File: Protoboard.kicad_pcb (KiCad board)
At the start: 2 copper layers, 99 x 138 mm, 76 parts, among them P1 CONN_01X08, P2 CONN_01X04, P3 CONN_01X05, P5 CONN_02X05, U1 LoLin_V3

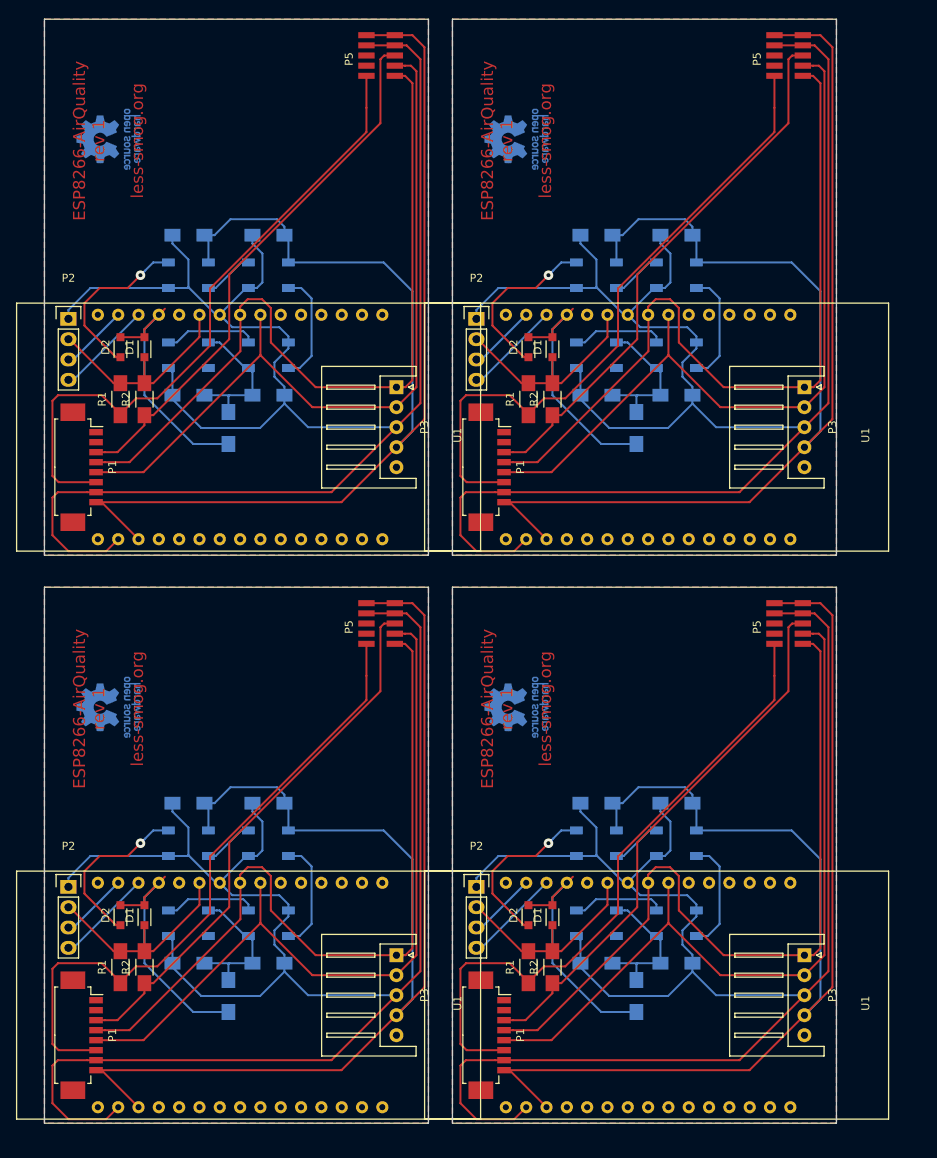
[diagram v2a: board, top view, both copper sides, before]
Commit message: Removed gerber files.
This is rev 2
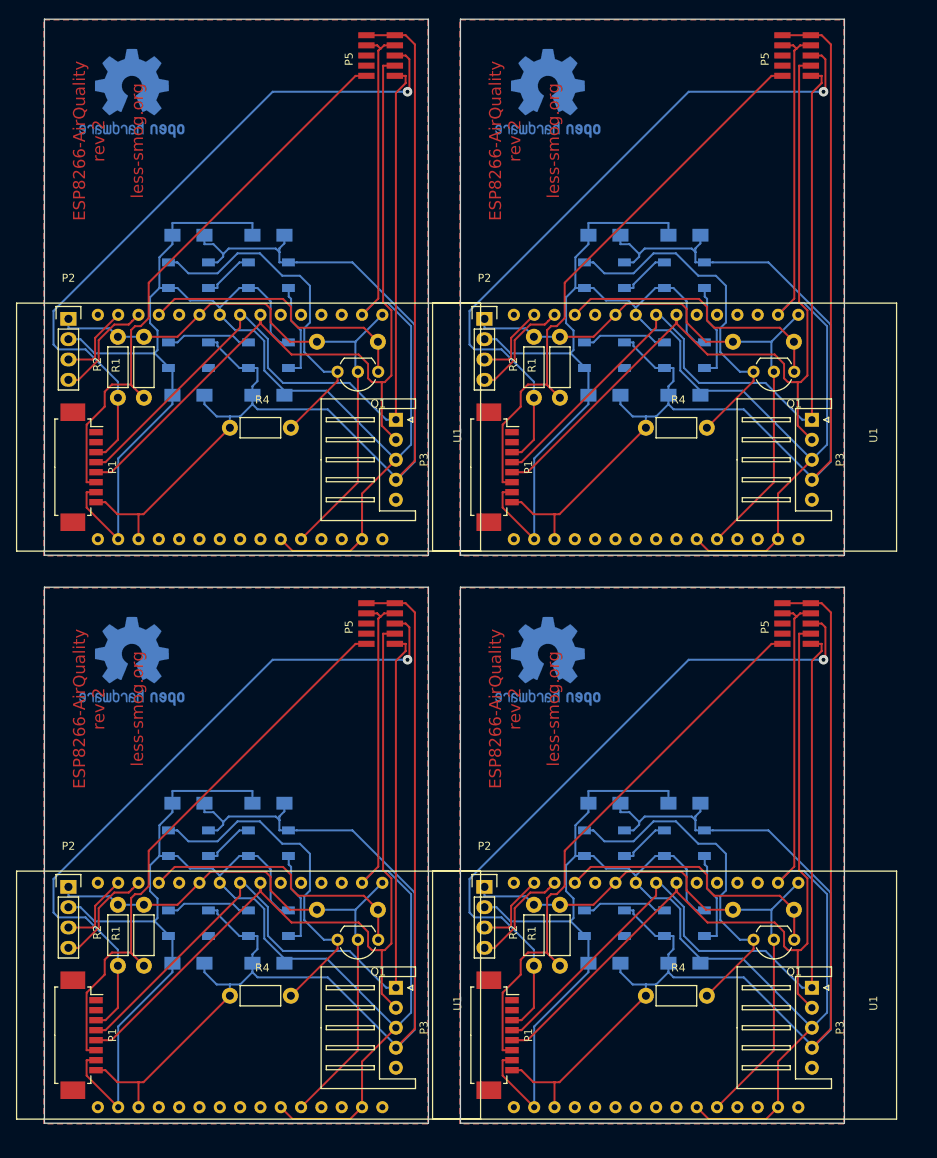
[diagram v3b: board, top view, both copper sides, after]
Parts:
- removed the C1 at (88.1, 117.9)
- removed the C1 at (88.1, 46.9)
- removed the C2 at (98.1, 117.9)
- removed the C2 at (98.1, 46.9)
- removed the C3 at (98.1, 137.9)
- removed the C3 at (98.1, 66.9)
- removed the C4 at (88.1, 137.9)
- removed the C4 at (88.1, 66.9)
- removed D1 (x4), D2 (x4): D, Diodes_SMD:SOD-323_HandSoldering
- removed the LED1 at (88.1, 122.9)
- removed the LED1 at (88.1, 51.9)
- removed the LED2 at (98.1, 122.9)
- removed the LED2 at (98.1, 51.9)
- removed the LED3 at (98.1, 132.9)
- removed the LED3 at (98.1, 61.9)
- removed the LED4 at (88.1, 132.9)
- removed the LED4 at (88.1, 61.9)
- removed the P1 at (75.1, 146.9)
- removed the P1 at (75.1, 75.9)
- removed the P2 at (73.1, 128.4)
- removed the P2 at (73.1, 57.4)
- removed the P3 at (114.1, 136.9)
- removed the P3 at (63.1, 136.9)
- removed the P3 at (114.1, 65.9)
- removed the P5 at (110.3, 92.9)
- removed the P5 at (110.3, 21.9)
- removed the R1 at (79.6, 138.4)
- removed the R1 at (28.6, 138.4)
- removed the R1 at (79.6, 67.4)
- removed the R1 at (28.6, 67.4)
- removed the R2 at (82.6, 138.4)
- removed the R2 at (31.6, 138.4)
- removed the R2 at (82.6, 67.4)
- removed the R2 at (31.6, 67.4)
- removed the R3 at (93.1, 142.0)
- removed the R3 at (42.1, 142.0)
- removed the R3 at (93.1, 71.0)
- removed the R3 at (42.1, 71.0)
- removed the REF*** at (78.1, 105.9)
- removed the REF*** at (27.1, 105.9)
- removed the REF*** at (78.1, 34.9)
- removed the REF*** at (27.1, 34.9)
- removed the U1 at (66.6, 157.7)
- removed the U1 at (66.6, 86.7)
- added C1: 100nF, Capacitors_SMD:C_1206_HandSoldering, B.Cu at (89.1, 117.9)
- added C1: 100nF, Capacitors_SMD:C_1206_HandSoldering, B.Cu at (89.1, 46.9)
- added C2: 100nF, Capacitors_SMD:C_1206_HandSoldering, B.Cu at (99.1, 117.9)
- added C2: 100nF, Capacitors_SMD:C_1206_HandSoldering, B.Cu at (99.1, 46.9)
- added C3: 100nF, Capacitors_SMD:C_1206_HandSoldering, B.Cu at (99.1, 137.9)
- added C3: 100nF, Capacitors_SMD:C_1206_HandSoldering, B.Cu at (99.1, 66.9)
- added C4: 100nF, Capacitors_SMD:C_1206_HandSoldering, B.Cu at (89.1, 137.9)
- added C4: 100nF, Capacitors_SMD:C_1206_HandSoldering, B.Cu at (89.1, 66.9)
- added LED1: WS2812B, LEDs:LED_WS2812B-PLCC4, B.Cu at (89.1, 122.9)
- added LED1: WS2812B, LEDs:LED_WS2812B-PLCC4, B.Cu at (89.1, 51.9)
- added LED2: WS2812B, LEDs:LED_WS2812B-PLCC4, B.Cu at (99.1, 122.9)
- added LED2: WS2812B, LEDs:LED_WS2812B-PLCC4, B.Cu at (99.1, 51.9)
- added LED3: WS2812B, LEDs:LED_WS2812B-PLCC4, B.Cu at (99.1, 132.9)
- added LED3: WS2812B, LEDs:LED_WS2812B-PLCC4, B.Cu at (99.1, 61.9)
- added LED4: WS2812B, LEDs:LED_WS2812B-PLCC4, B.Cu at (89.1, 132.9)
- added LED4: WS2812B, LEDs:LED_WS2812B-PLCC4, B.Cu at (89.1, 61.9)
- added P1: CONN_01X08, Connectors_Molex:Molex_PicoBlade_53261-0871_08x1.25mm_Angled, F.Cu at (76.1, 146.9)
- added P1: CONN_01X08, Connectors_Molex:Molex_PicoBlade_53261-0871_08x1.25mm_Angled, F.Cu at (76.1, 75.9)
- added P2: CONN_01X04, Pin_Headers:Pin_Header_Straight_1x04, F.Cu at (74.1, 128.4)
- added P2: CONN_01X04, Pin_Headers:Pin_Header_Straight_1x04, F.Cu at (74.1, 57.4)
- added P3: CONN_01X05, Connectors_JST:JST_XH_S05B-XH-A_05x2.50mm_Angled, F.Cu at (115.0, 141.0)
- added P3: CONN_01X05, Connectors_JST:JST_XH_S05B-XH-A_05x2.50mm_Angled, F.Cu at (63.0, 141.0)
- added P3: CONN_01X05, Connectors_JST:JST_XH_S05B-XH-A_05x2.50mm_Angled, F.Cu at (115.0, 70.0)
- added P5: CONN_02X05, Amphenol:Amphenol, F.Cu at (111.3, 92.9)
- added P5: CONN_02X05, Amphenol:Amphenol, F.Cu at (111.3, 21.9)
- added Q1: 2N7000, TO_SOT_Packages_THT:TO-92_Inline_Wide, F.Cu at (112.8, 135.0)
- added Q1: 2N7000, TO_SOT_Packages_THT:TO-92_Inline_Wide, F.Cu at (60.8, 135.0)
- added Q1: 2N7000, TO_SOT_Packages_THT:TO-92_Inline_Wide, F.Cu at (112.8, 64.0)
- added Q1: 2N7000, TO_SOT_Packages_THT:TO-92_Inline_Wide, F.Cu at (60.8, 64.0)
- added R1: 10k, Resistors_THT:Resistor_Horizontal_RM7mm, F.Cu at (83.5, 138.2)
- added R1: 10k, Resistors_THT:Resistor_Horizontal_RM7mm, F.Cu at (31.5, 138.2)
- added R1: 10k, Resistors_THT:Resistor_Horizontal_RM7mm, F.Cu at (83.5, 67.2)
- added R1: 10k, Resistors_THT:Resistor_Horizontal_RM7mm, F.Cu at (31.5, 67.2)
- added R2: 10k, Resistors_THT:Resistor_Horizontal_RM7mm, F.Cu at (80.2, 138.2)
- added R2: 10k, Resistors_THT:Resistor_Horizontal_RM7mm, F.Cu at (28.2, 138.2)
- added R2: 10k, Resistors_THT:Resistor_Horizontal_RM7mm, F.Cu at (80.2, 67.2)
- added R2: 10k, Resistors_THT:Resistor_Horizontal_RM7mm, F.Cu at (28.2, 67.2)
- added R3: 10k, Resistors_THT:Resistor_Horizontal_RM7mm, B.Cu at (105.1, 131.2)
- added R3: 10k, Resistors_THT:Resistor_Horizontal_RM7mm, B.Cu at (53.1, 131.2)
- added R3: 10k, Resistors_THT:Resistor_Horizontal_RM7mm, B.Cu at (105.1, 60.2)
- added R3: 10k, Resistors_THT:Resistor_Horizontal_RM7mm, B.Cu at (53.1, 60.2)
- added R4: 10k, Resistors_THT:Resistor_Horizontal_RM7mm, F.Cu at (94.2, 142.0)
- added R4: 10k, Resistors_THT:Resistor_Horizontal_RM7mm, F.Cu at (42.2, 142.0)
- added R4: 10k, Resistors_THT:Resistor_Horizontal_RM7mm, F.Cu at (94.2, 71.0)
- added R4: 10k, Resistors_THT:Resistor_Horizontal_RM7mm, F.Cu at (42.2, 71.0)
- added REF***: OSHW-Logo2_14.6x12mm_Copper, Symbols:OSHW-Logo2_14.6x12mm_Copper, B.Cu at (82.0, 100.2)
- added REF***: OSHW-Logo2_14.6x12mm_Copper, Symbols:OSHW-Logo2_14.6x12mm_Copper, B.Cu at (30.0, 100.2)
- added REF***: OSHW-Logo2_14.6x12mm_Copper, Symbols:OSHW-Logo2_14.6x12mm_Copper, B.Cu at (82.0, 29.2)
- added REF***: OSHW-Logo2_14.6x12mm_Copper, Symbols:OSHW-Logo2_14.6x12mm_Copper, B.Cu at (30.0, 29.2)
- added U1: LoLin_V3, LoLin:LoLin, F.Cu at (67.6, 157.7)
- added U1: LoLin_V3, LoLin:LoLin, F.Cu at (67.6, 86.7)
- moved P3 4.07 mm to (63.0, 70.0)
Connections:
- P2 pad 1: GND -> +3.3V (x2)
- P2 pad 2: +3.3V -> GND (x2)
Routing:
- net +3.3V: track 111.1 -> 298.7 mm
- net LED: track 86.2 -> 176.6 mm, vias 4 -> 0
- net RESET: track 272.2 -> 346.3 mm, vias 0 -> 4
- net SET: track 326.6 -> 287.0 mm
- net +5V: track 727.3 -> 757.6 mm
- net GND: track 858.3 -> 879.8 mm
- net DIN: track 127.8 -> 140.7 mm
- net RXD: track 389.5 -> 399.1 mm
- net Net-(LED2-Pad2): track 56.6 -> 48.7 mm
- net SCL: track 48.5 -> 54.2 mm
- net SDA: track 34.1 -> 39.8 mm
- net Net-(LED3-Pad2): track 46.4 -> 42.7 mm
- net Net-(LED1-Pad2): track 25.3 -> 26.4 mm
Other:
- board size 99 x 138 mm -> 100 x 138 mm
- board text added: "ESP8266-AirQuality rev 2 less-smog.org"
- board text removed: "ESP8266-AirQuality rev 1 less-smog.org"
